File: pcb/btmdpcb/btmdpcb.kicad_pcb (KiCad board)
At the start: 2 copper layers, 51 parts, among them J2 ANT, Q1 BSD235C, Q2 2N7000, Q3 2N7000, Q4 BSD235C, Q5 AO3401A, Q6 BSD235C, Q7 2N7000, Q8 BSD235N, T1 ED8_4, T2 ED8_4, U2 TP4057, U3 ME6211C33M5

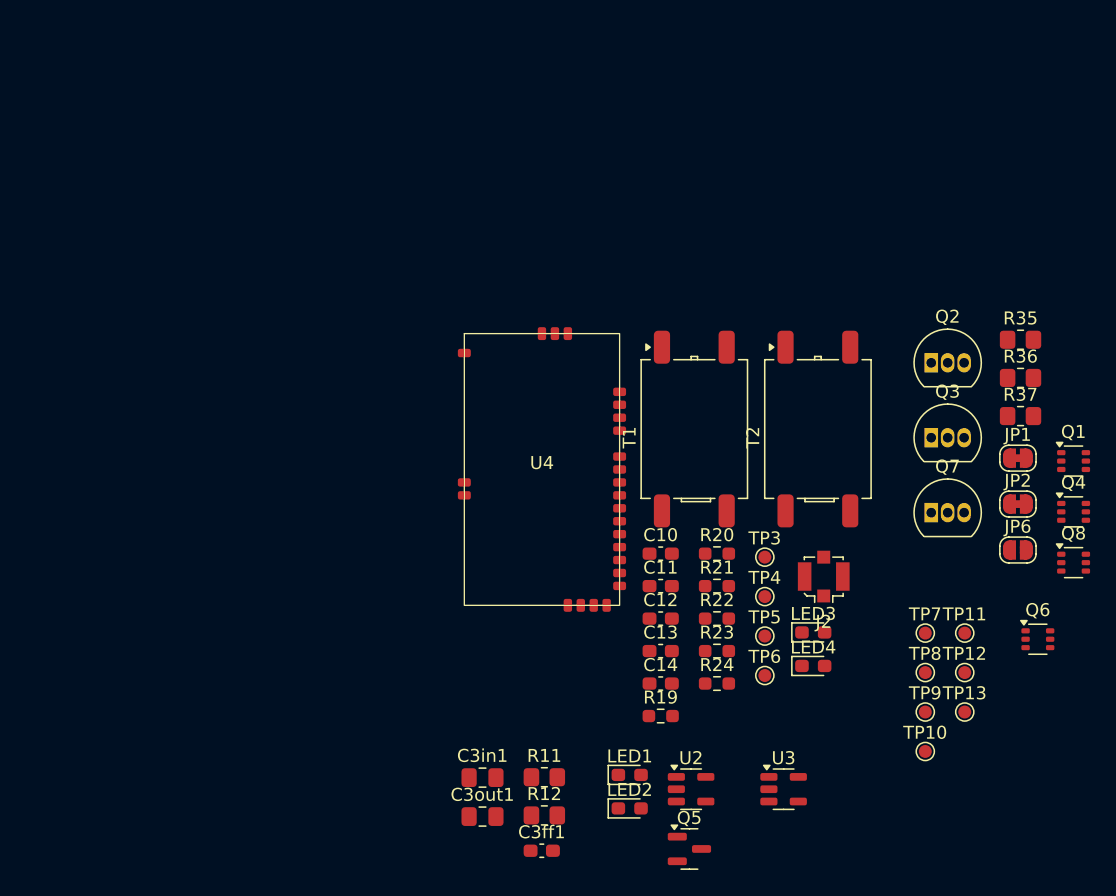
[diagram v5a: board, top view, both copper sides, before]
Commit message: Add missing libraries, assign all footprints
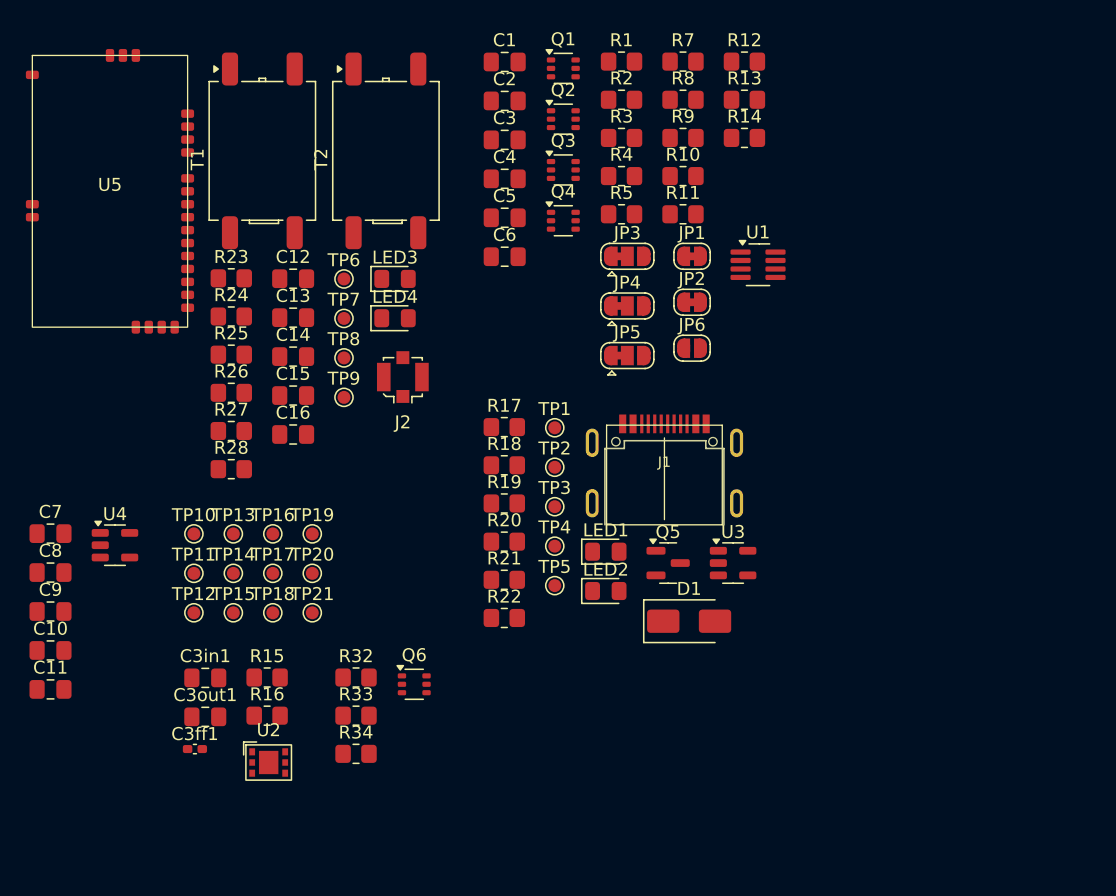
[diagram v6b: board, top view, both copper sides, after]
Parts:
- removed Q7: 2N7000, Package_TO_SOT_THT:TO-92_Inline
- removed Q8: BSD235N, Package_TO_SOT_SMD:SOT-363_SC-70-6
- removed R35, R36, R37: R, Resistor_SMD:R_0805_2012Metric_Pad1.20x1.40mm_HandSolder
- added C1: C, Capacitor_SMD:C_0805_2012Metric_Pad1.18x1.45mm_HandSolder, F.Cu at (62.5, 25.9)
- added C15: 1u, Capacitor_SMD:C_0805_2012Metric_Pad1.18x1.45mm_HandSolder, F.Cu at (46.1, 51.6)
- added C16: 100n, Capacitor_SMD:C_0805_2012Metric_Pad1.18x1.45mm_HandSolder, F.Cu at (46.1, 54.6)
- added C2: 1u, Capacitor_SMD:C_0805_2012Metric_Pad1.18x1.45mm_HandSolder, F.Cu at (62.5, 28.9)
- added C3: 10u, Capacitor_SMD:C_0805_2012Metric_Pad1.18x1.45mm_HandSolder, F.Cu at (62.5, 31.9)
- added C4: 100n, Capacitor_SMD:C_0805_2012Metric_Pad1.18x1.45mm_HandSolder, F.Cu at (62.5, 34.9)
- added C5: 100n, Capacitor_SMD:C_0805_2012Metric_Pad1.18x1.45mm_HandSolder, F.Cu at (62.5, 37.9)
- added C6: 1u or more, Capacitor_SMD:C_0805_2012Metric_Pad1.18x1.45mm_HandSolder, F.Cu at (62.5, 40.9)
- added C7: 10u, Capacitor_SMD:C_0805_2012Metric_Pad1.18x1.45mm_HandSolder, F.Cu at (27.4, 62.3)
- added C8: 100n, Capacitor_SMD:C_0805_2012Metric_Pad1.18x1.45mm_HandSolder, F.Cu at (27.4, 65.3)
- added C9: 1u, Capacitor_SMD:C_0805_2012Metric_Pad1.18x1.45mm_HandSolder, F.Cu at (27.4, 68.3)
- added D1: GS1A, Diode_SMD:D_SMA, F.Cu at (76.7, 69.1)
- added J1: USB_C_Receptacle_USB2.0_14P, usb:TYPE-C-31-M-14, F.Cu at (74.8, 58.9)
- added JP3: SolderJumper_3_Bridged12, Jumper:SolderJumper-3_P1.3mm_Bridged12_RoundedPad1.0x1.5mm, F.Cu at (72.0, 40.9)
- added JP4: SolderJumper_3_Bridged12, Jumper:SolderJumper-3_P1.3mm_Bridged12_RoundedPad1.0x1.5mm, F.Cu at (72.0, 44.7)
- added JP5: SolderJumper_3_Bridged12, Jumper:SolderJumper-3_P1.3mm_Bridged12_RoundedPad1.0x1.5mm, F.Cu at (72.0, 48.5)
- added R1: 10k, Resistor_SMD:R_0805_2012Metric_Pad1.20x1.40mm_HandSolder, F.Cu at (71.5, 25.8)
- added R10: 100k, Resistor_SMD:R_0805_2012Metric_Pad1.20x1.40mm_HandSolder, F.Cu at (76.3, 34.7)
- added R13: 100k, Resistor_SMD:R_0805_2012Metric_Pad1.20x1.40mm_HandSolder, F.Cu at (81.0, 28.8)
- added R14: 100k, Resistor_SMD:R_0805_2012Metric_Pad1.20x1.40mm_HandSolder, F.Cu at (81.0, 31.7)
- added R15: 100k, Resistor_SMD:R_0805_2012Metric_Pad1.20x1.40mm_HandSolder, F.Cu at (44.1, 73.4)
- added R16: 115k, Resistor_SMD:R_0805_2012Metric_Pad1.20x1.40mm_HandSolder, F.Cu at (44.1, 76.4)
- added R17: 5k1, Resistor_SMD:R_0805_2012Metric_Pad1.20x1.40mm_HandSolder, F.Cu at (62.5, 54.1)
- added R18: 5k1, Resistor_SMD:R_0805_2012Metric_Pad1.20x1.40mm_HandSolder, F.Cu at (62.5, 57.0)
- added R2: 10k, Resistor_SMD:R_0805_2012Metric_Pad1.20x1.40mm_HandSolder, F.Cu at (71.5, 28.8)
- added R25: 5k1, Resistor_SMD:R_0805_2012Metric_Pad1.20x1.40mm_HandSolder, F.Cu at (41.4, 48.5)
- added R26: 5k1, Resistor_SMD:R_0805_2012Metric_Pad1.20x1.40mm_HandSolder, F.Cu at (41.4, 51.4)
- added R27: 100R, Resistor_SMD:R_0805_2012Metric_Pad1.20x1.40mm_HandSolder, F.Cu at (41.4, 54.4)
- added R28: 100R, Resistor_SMD:R_0805_2012Metric_Pad1.20x1.40mm_HandSolder, F.Cu at (41.4, 57.3)
- added R3: 330k, Resistor_SMD:R_0805_2012Metric_Pad1.20x1.40mm_HandSolder, F.Cu at (71.5, 31.7)
- added R32: 100k, Resistor_SMD:R_0805_2012Metric_Pad1.20x1.40mm_HandSolder, F.Cu at (51.0, 73.4)
- added R33: 100k, Resistor_SMD:R_0805_2012Metric_Pad1.20x1.40mm_HandSolder, F.Cu at (51.0, 76.4)
- added R34: 100k, Resistor_SMD:R_0805_2012Metric_Pad1.20x1.40mm_HandSolder, F.Cu at (51.0, 79.3)
- added R4: 150k, Resistor_SMD:R_0805_2012Metric_Pad1.20x1.40mm_HandSolder, F.Cu at (71.5, 34.7)
- added R5: 220k, Resistor_SMD:R_0805_2012Metric_Pad1.20x1.40mm_HandSolder, F.Cu at (71.5, 37.6)
- added R7: 100k, Resistor_SMD:R_0805_2012Metric_Pad1.20x1.40mm_HandSolder, F.Cu at (76.3, 25.8)
- added R8: 100k, Resistor_SMD:R_0805_2012Metric_Pad1.20x1.40mm_HandSolder, F.Cu at (76.3, 28.8)
- added R9: 10k, Resistor_SMD:R_0805_2012Metric_Pad1.20x1.40mm_HandSolder, F.Cu at (76.3, 31.7)
- added TP1: VUSB, TestPoint:TestPoint_Pad_D1.0mm, F.Cu at (66.4, 54.1)
- added TP14: TestPoint, TestPoint:TestPoint_Pad_D1.0mm, F.Cu at (41.5, 65.4)
- added TP15: TestPoint, TestPoint:TestPoint_Pad_D1.0mm, F.Cu at (41.5, 68.4)
- added TP16: TestPoint, TestPoint:TestPoint_Pad_D1.0mm, F.Cu at (44.6, 62.3)
- added TP17: TestPoint, TestPoint:TestPoint_Pad_D1.0mm, F.Cu at (44.6, 65.4)
- added TP18: TestPoint, TestPoint:TestPoint_Pad_D1.0mm, F.Cu at (44.6, 68.4)
- added TP19: TestPoint, TestPoint:TestPoint_Pad_D1.0mm, F.Cu at (47.6, 62.3)
- added TP2: VUSB, TestPoint:TestPoint_Pad_D1.0mm, F.Cu at (66.4, 57.2)
- added TP20: TestPoint, TestPoint:TestPoint_Pad_D1.0mm, F.Cu at (47.6, 65.4)
- added TP21: TestPoint, TestPoint:TestPoint_Pad_D1.0mm, F.Cu at (47.6, 68.4)
- added U1: LM393, Package_TO_SOT_SMD:SOT-23-8_Handsoldering, F.Cu at (82.1, 41.5)
- added U5: ~, bt_audio:bt_audio_smd, F.Cu at (32.0, 35.9)
- C10, C12, C13: footprint Capacitor_SMD:C_0603_1608Metric_Pad1.08x0.95mm_HandSolder -> Capacitor_SMD:C_0805_2012Metric_Pad1.18x1.45mm_HandSolder
- C11: value 1u -> 100n; footprint Capacitor_SMD:C_0603_1608Metric_Pad1.08x0.95mm_HandSolder -> Capacitor_SMD:C_0805_2012Metric_Pad1.18x1.45mm_HandSolder
- C14: value 100n -> 1u; footprint Capacitor_SMD:C_0603_1608Metric_Pad1.08x0.95mm_HandSolder -> Capacitor_SMD:C_0805_2012Metric_Pad1.18x1.45mm_HandSolder
- C3ff1: footprint Capacitor_SMD:C_0603_1608Metric_Pad1.08x0.95mm_HandSolder -> Capacitor_SMD:C_0402_1005Metric_Pad0.74x0.62mm_HandSolder
- LED1, LED2, LED3, LED4: footprint LED_SMD:LED_0603_1608Metric_Pad1.05x0.95mm_HandSolder -> LED_SMD:LED_0805_2012Metric_Pad1.15x1.40mm_HandSolder
- Q1: value BSD235C -> BSD235N
- Q2: value 2N7000 -> BSD235C; footprint Package_TO_SOT_THT:TO-92_Inline -> Package_TO_SOT_SMD:SOT-363_SC-70-6
- Q3: value 2N7000 -> BSD235N; footprint Package_TO_SOT_THT:TO-92_Inline -> Package_TO_SOT_SMD:SOT-363_SC-70-6
- R12: value 115k -> 100k
- R19, R20: value 5k1 -> 330R; footprint Resistor_SMD:R_0603_1608Metric_Pad0.98x0.95mm_HandSolder -> Resistor_SMD:R_0805_2012Metric_Pad1.20x1.40mm_HandSolder
- R21: value 5k1 -> TBD; footprint Resistor_SMD:R_0603_1608Metric_Pad0.98x0.95mm_HandSolder -> Resistor_SMD:R_0805_2012Metric_Pad1.20x1.40mm_HandSolder
- R22: value 5k1 -> 100k; footprint Resistor_SMD:R_0603_1608Metric_Pad0.98x0.95mm_HandSolder -> Resistor_SMD:R_0805_2012Metric_Pad1.20x1.40mm_HandSolder
- R23, R24: value 100R -> 5k1; footprint Resistor_SMD:R_0603_1608Metric_Pad0.98x0.95mm_HandSolder -> Resistor_SMD:R_0805_2012Metric_Pad1.20x1.40mm_HandSolder
- TP3: value TestPoint -> VUSB
- TP4: value TestPoint -> BAT+
- TP5: value LED1 -> BAT-
- TP6: value LED2 -> TestPoint
- TP8: value TestPoint -> LED1
- TP9: value TestPoint -> LED2
- U2: value TP4057 -> Würth 171010502; footprint Package_TO_SOT_SMD:TSOT-23-5 -> MagIC_SMD_Wurth:U_Wurth_WPME-VDMM_171010502
- U3: value ME6211C33M5 -> TP4057; footprint Package_TO_SOT_SMD:SOT-23-5 -> Package_TO_SOT_SMD:TSOT-23-5
- U4: value ~ -> ME6211C33M5; footprint bt_audio:bt_audio_smd -> Package_TO_SOT_SMD:SOT-23-5
- moved R12 60.3 mm to (81.0, 25.8)
- moved TP11 59.8 mm to (38.5, 65.4)
- moved TP12 59.8 mm to (38.5, 68.4)
- moved TP10 59.0 mm to (38.5, 62.3)
- moved TP13 58.2 mm to (41.5, 62.3)
- moved TP7 51.1 mm to (50.1, 45.7)
- moved TP8 51.1 mm to (50.1, 48.7)
- moved TP9 51.1 mm to (50.1, 51.8)
- moved Q1 49.8 mm to (67.0, 26.4)
- moved Q6 48.3 mm to (55.5, 74.0)
- moved C11 47.8 mm to (27.4, 74.3)
- moved C10 47.7 mm to (27.4, 71.3)
- moved R23 47.3 mm to (41.4, 42.6)
- moved R24 47.0 mm to (41.4, 45.5)
- moved Q4 45.4 mm to (67.0, 38.1)
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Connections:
- C10 pad 1: Net-(C10-Pad1) -> +3V3
- C10 pad 2: Net-(U4-L+) -> GND
- C11 pad 1: Net-(C11-Pad1) -> +3V3
- C11 pad 2: Net-(U4-L-) -> GND
- C12 pad 2: Net-(U4-R-) -> Net-(U5-L+)
- C13 pad 2: Net-(U4-R+) -> Net-(U5-L-)
- C14 pad 1: +3V3 -> Net-(C14-Pad1)
- C14 pad 2: GND -> Net-(U5-R-)
- C3ff1 pad 2: Net-(U1-FB) -> Net-(U2-FB)
- Q1 pad 2: /HOLD -> Net-(Q1A-G1)
- Q1 pad 3: /REC -> unconnected-(Q1B-D2-Pad3)
- Q1 pad 4: +BATT -> unconnected-(Q1B-S2-Pad4)
- Q1 pad 5: /~{REC} -> unconnected-(Q1B-G2-Pad5)
- Q1 pad 6: /KICKSTART/BT_BTN -> Net-(Q1A-D1)
- Q2 pad 2: /KICKSTART/BT_BTN -> /HOLD
- Q2 pad 3: ~{EN_1V5} -> /REC
- Q3 pad 2: VDD -> /KICKSTART/BT_BTN
- Q5 pad 3: Net-(BT1-+) -> Net-(Q5-D)
- R11 pad 1: +1V5 -> VDD
- R11 pad 2: Net-(U1-FB) -> GND
- R12 pad 1: Net-(U1-FB) -> +BATT
- R12 pad 2: GND -> ~{EN_1V5}
- R19 pad 1: Net-(R19-Pad1) -> VBUS
- R19 pad 2: Net-(C10-Pad1) -> Net-(LED1-A)
- R20 pad 1: Net-(R20-Pad1) -> VBUS
- R20 pad 2: Net-(C11-Pad1) -> Net-(LED2-A)
- R21 pad 1: Net-(R21-Pad1) -> Net-(U3-PROG)
- R21 pad 2: Net-(C12-Pad1) -> GND
- R22 pad 1: Net-(R22-Pad1) -> VBUS
- R22 pad 2: Net-(C13-Pad1) -> GND
- R23 pad 1: Net-(U4-LED1) -> Net-(R23-Pad1)
- R23 pad 2: Net-(LED3-K) -> Net-(C12-Pad1)
- R24 pad 1: Net-(U4-LED2) -> Net-(R24-Pad1)
- R24 pad 2: Net-(LED4-K) -> Net-(C13-Pad1)
- T1 pad 3: Net-(R20-Pad1) -> Net-(R24-Pad1)
- T1 pad 4: Net-(R19-Pad1) -> Net-(R23-Pad1)
- T2 pad 3: Net-(R21-Pad1) -> Net-(R25-Pad1)
- T2 pad 4: Net-(R22-Pad1) -> Net-(R26-Pad1)
- TP10 pad 1: /MD unit (MZ-N505)/~{BTN_REC}_IN -> +1V5
- TP11 pad 1: /MD unit (MZ-N505)/~{BTN_PAUSE}_IN -> GND
- TP12 pad 1: /~{REC} -> /MD unit (MZ-N505)/~{BTN_PAUSE}_IN
- TP13 pad 1: /~{HOLD} -> /MD unit (MZ-N505)/~{SW_HOLD}_IN
- TP3 pad 1: Net-(U4-BAT+) -> VBUS
- TP4 pad 1: /bt_module/PWR_EN -> Net-(Q5-D)
- TP5 pad 1: Net-(LED3-K) -> GND
- TP6 pad 1: Net-(LED4-K) -> Net-(U5-BAT+)
- TP7 pad 1: /MD unit (MZ-N505)/~{BTN_PAUSE}_IN -> /bt_module/PWR_EN
- TP8 pad 1: /MD unit (MZ-N505)/~{SW_HOLD}_IN -> Net-(LED3-K)
- TP9 pad 1: VDD -> Net-(LED4-K)
- U2 pad 1: Net-(LED2-K) -> +1V5
- U2 pad 2: GND -> /power_we/MODE
- U2 pad 3: Net-(BT1-+) -> Net-(U2-FB)
- U2 pad 4: VBUS -> /power_we/Vin
- U2 pad 5: Net-(LED1-K) -> /power_we/EN
- U3 pad 1: /power_3v3/Vin -> Net-(LED2-K)
- U3 pad 3: /power_3v3/EN -> Net-(Q5-D)
- U3 pad 4: unconnected-(U3-NC-Pad4) -> VBUS
- U3 pad 5: +3V3 -> Net-(LED1-K)
- U4 pad 1: GND -> /power_3v3/Vin
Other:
- board outline added: 9.2 x 6.5 mm

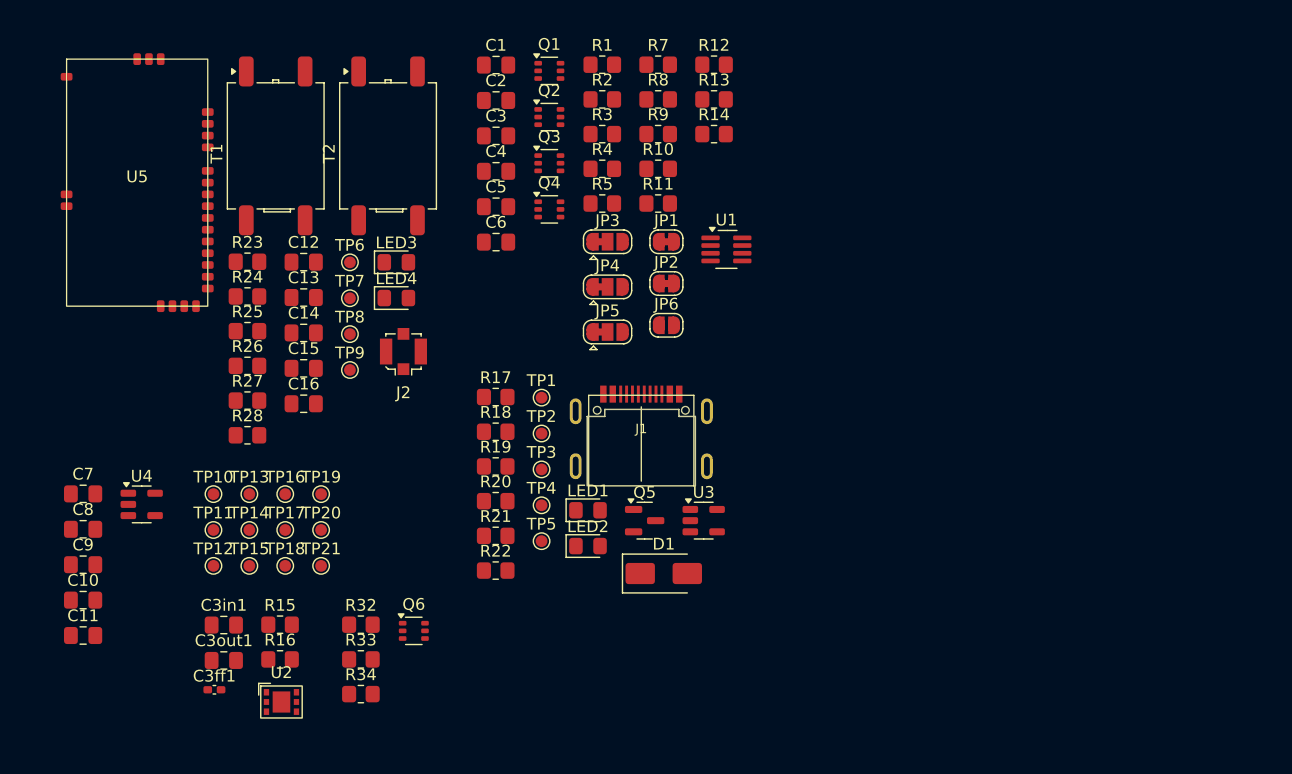
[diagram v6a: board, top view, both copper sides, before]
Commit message: Correct footprints, fix issues on update PCB from schematic
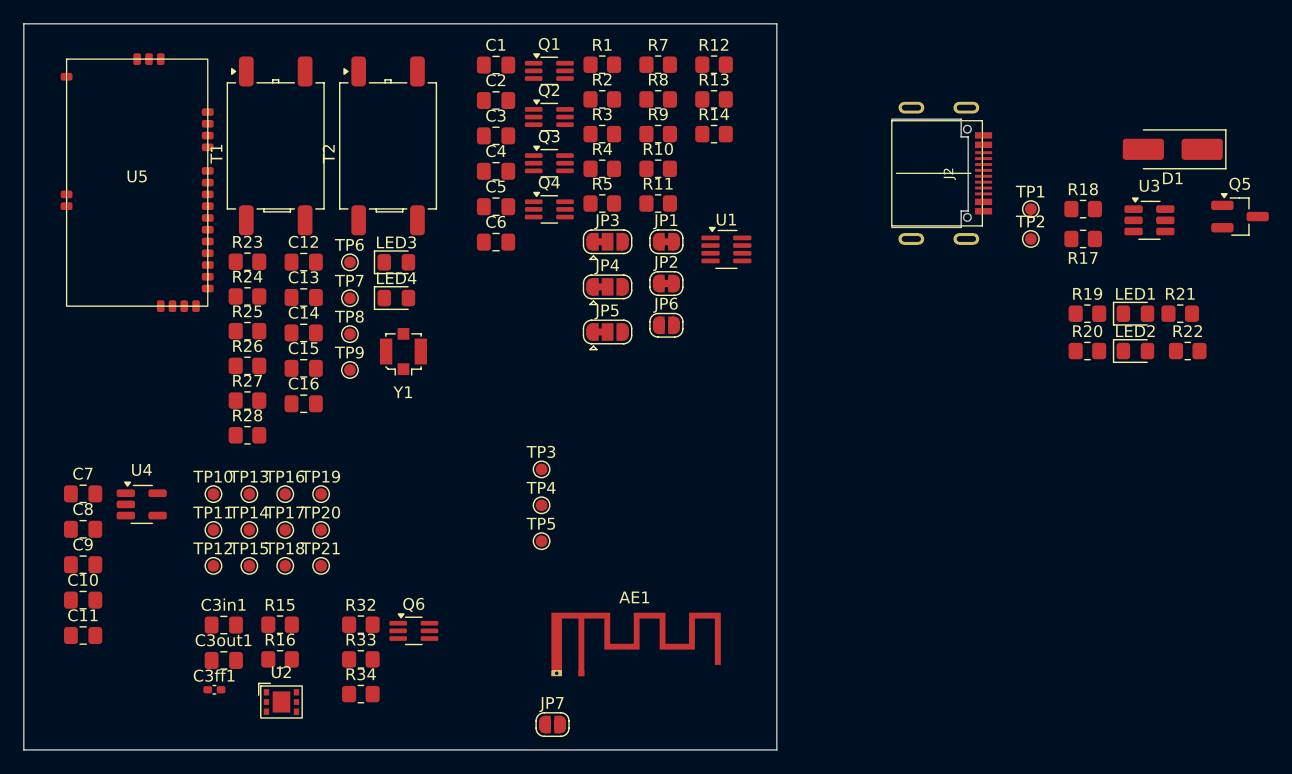
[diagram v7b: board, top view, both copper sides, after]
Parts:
- removed J1: USB_C_Receptacle_USB2.0_14P, usb:TYPE-C-31-M-14
- added AE1: Antenna_Shield, RF_Antenna:Texas_SWRA117D_2.4GHz_Right, F.Cu at (69.7, 77.6)
- added J2: USB_C_Receptacle_USB2.0_16P, usb:TYPE-C-31-M-14, F.Cu at (98.8, 35.1)
- added JP7: SolderJumper_2_Open, Jumper:SolderJumper-2_P1.3mm_Open_RoundedPad1.0x1.5mm, F.Cu at (67.3, 81.9)
- D1: footprint Diode_SMD:D_SMA -> Diode_SMD:D_SMA_Handsoldering
- Q1, Q2, Q3, Q4, Q6: footprint Package_TO_SOT_SMD:SOT-363_SC-70-6 -> Package_TO_SOT_SMD:SOT-363_SC-70-6_Handsoldering
- Q5: footprint Package_TO_SOT_SMD:SOT-23 -> Package_TO_SOT_SMD:SOT-23_Handsoldering
- U3: footprint Package_TO_SOT_SMD:TSOT-23-5 -> Package_TO_SOT_SMD:SOT-23-6_Handsoldering
- U4: footprint Package_TO_SOT_SMD:SOT-23-5 -> Package_TO_SOT_SMD:SOT-23-5_HandSoldering
- moved R22 61.7 mm to (121.3, 50.2)
- moved R21 61.2 mm to (120.7, 47.0)
- moved Q5 56.8 mm to (125.7, 38.7)
- moved D1 56.3 mm to (120.0, 33.0), turned to 180 degrees
- moved R18 53.4 mm to (112.4, 38.1)
- moved R19 51.9 mm to (112.8, 47.0)
- moved R20 51.9 mm to (112.8, 50.2)
- moved R17 51.7 mm to (112.4, 40.6), turned to 180 degrees
- moved LED1 49.4 mm to (116.8, 47.0)
- moved LED2 49.4 mm to (116.8, 50.2)
- moved U3 45.7 mm to (118.0, 39.1)
- moved TP2 44.8 mm to (108.0, 40.6)
- moved TP1 44.6 mm to (108.0, 38.1)
- renumbered J2 to Y1
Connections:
- net Net-(Q5-D) renamed /supply/BAT+
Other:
- board size 9.2 x 6.5 mm -> 64 x 61.7 mm
- copper layers 2 -> 4

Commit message: Layout PCB
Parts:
- removed the C1 at (62.5, 25.9)
- removed the C5 at (62.5, 37.9)
- removed the TP12 at (38.5, 68.4)
- removed the TP15 at (41.5, 68.4)
- removed the TP19 at (47.6, 62.3)
- added C18: 100n, Capacitor_SMD:C_0805_2012Metric_Pad1.18x1.45mm_HandSolder, F.Cu at (145.4, 60.3)
- added C20: 100n, Capacitor_SMD:C_0805_2012Metric_Pad1.18x1.45mm_HandSolder, F.Cu at (158.8, 49.5)
- added C3: 10u, Capacitor_SMD:C_0805_2012Metric_Pad1.18x1.45mm_HandSolder, F.Cu at (115.6, 46.4)
- added JP10: L_SKIP, Jumper:SolderJumper-2_P1.3mm_Open_RoundedPad1.0x1.5mm, F.Cu at (130.2, 81.3)
- added JP12: USB_PWR, Jumper:SolderJumper-2_P1.3mm_Open_RoundedPad1.0x1.5mm, F.Cu at (140.8, 60.3)
- added JP7: SHLD2GND, Jumper:SolderJumper-2_P1.3mm_Open_RoundedPad1.0x1.5mm, F.Cu at (100.3, 59.1)
- added JP8: R_SKIP, Jumper:SolderJumper-2_P1.3mm_Open_RoundedPad1.0x1.5mm, F.Cu at (130.2, 68.6)
- added JP9: AGND_SKIP, Jumper:SolderJumper-3_P1.3mm_Open_RoundedPad1.0x1.5mm, F.Cu at (130.2, 74.9)
- added TP10: 3V3_IN, TestPoint:TestPoint_Pad_D1.0mm, F.Cu at (144.9, 45.1)
- added TP11: 3V3_OUT, TestPoint:TestPoint_Pad_D1.0mm, F.Cu at (144.9, 52.7)
- added TP22: BT_L+, TestPoint:TestPoint_Pad_D1.0mm, F.Cu at (148.6, 70.5)
- added TP23: BT_L-, TestPoint:TestPoint_Pad_D1.0mm, F.Cu at (148.6, 67.9)
- added TP24: BT_R-, TestPoint:TestPoint_Pad_D1.0mm, F.Cu at (148.6, 65.4)
- added TP25: BT_R+, TestPoint:TestPoint_Pad_D1.0mm, F.Cu at (148.6, 62.9)
- added TP26: BT_USB_IN, TestPoint:TestPoint_Pad_D1.0mm, F.Cu at (148.6, 60.3)
- added TP27: BT_3V3, TestPoint:TestPoint_Pad_D1.0mm, F.Cu at (165.1, 64.1)
- added TP28: GND, TestPoint:TestPoint_Pad_D1.0mm, F.Cu at (165.1, 54.6)
- added TP29: BT_BTN, TestPoint:TestPoint_Pad_D1.0mm, F.Cu at (154.9, 49.5)
- added TP3: GND, TestPoint:TestPoint_Pad_D1.0mm, F.Cu at (109.2, 61.6)
- added TP7: VSUPPLY, TestPoint:TestPoint_Pad_D1.0mm, F.Cu at (128.3, 49.5)
- added TP8: 1V5_IN, TestPoint:TestPoint_Pad_D1.0mm, F.Cu at (126.2, 58.3)
- added TP9: 1V5_OUT, TestPoint:TestPoint_Pad_D1.0mm, F.Cu at (134.2, 57.0)
- AE1: footprint RF_Antenna:Texas_SWRA117D_2.4GHz_Right -> RF_Antenna:Texas_SWRA117D_2.4GHz_Left
- C4: value 100n -> 10u
- C6: value 1u or more -> 1u
- JP1: value SolderJumper_2_Bridged -> 1V5_IN
- JP11: renamed from JP7; value SolderJumper_2_Open -> ANT
- JP2: value SolderJumper_2_Bridged -> 3V3_IN
- JP3: value SolderJumper_3_Bridged12 -> 1V5_EN
- JP4: value SolderJumper_3_Bridged12 -> 3V3_EN
- JP5: value SolderJumper_3_Bridged12 -> 3V3_MODE
- JP6: value SolderJumper_2_Open -> VBUS_EN
- R19: renamed from R21; value TBD -> 1k6
- TP1: value VUSB -> D-
- TP12: renamed from TP10; value TestPoint -> 1V5
- TP13: renamed from TP11; value TestPoint -> GND
- TP15: renamed from TP13; value TestPoint -> HOLD
- TP16: renamed from TP17; value TestPoint -> L
- TP17: renamed from TP16; value TestPoint -> R
- TP18: value TestPoint -> AGND
- TP19: renamed from TP14; value TestPoint -> DVDD
- TP2: value VUSB -> D+
- TP20: value TestPoint -> REC
- TP21: value TestPoint -> HOLD
- TP30: renamed from TP8; value LED1 -> BT_LED1
- TP31: renamed from TP9; value LED2 -> BT_LED2
- TP32: renamed from TP6; value TestPoint -> BT_BAT+
- TP33: renamed from TP7; value TestPoint -> BT_CE
- TP5: renamed from TP4; value BAT+ -> +
- TP6: renamed from TP5; value BAT- -> -
- moved U5 127.6 mm to (156.8, 62.2), turned to 180 degrees
- moved C13 120.8 mm to (145.5, 48.9), turned to -90 degrees
- moved C19 119.1 mm to (165.1, 60.3), turned to 90 degrees
- moved C12 115.2 mm to (141.1, 52.7)
- moved C9 115.0 mm to (141.1, 45.1)
- moved C10 111.1 mm to (136.6, 45.1)
- moved C11 110.3 mm to (136.6, 52.7), turned to 180 degrees
- moved U4 109.0 mm to (140.4, 48.9)
- moved Y1 107.3 mm to (158.8, 76.2), turned to -90 degrees
- moved R29 104.1 mm to (145.4, 55.2), turned to 180 degrees
- moved R30 104.1 mm to (145.4, 57.8)
- moved R25 103.4 mm to (141.0, 70.5)
- moved C14 103.1 mm to (145.4, 70.5)
- moved TP32 102.6 mm to (152.4, 49.5), turned to 180 degrees
- moved R26 102.1 mm to (141.0, 67.9)
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- renumbered C2 to C1, C8 to C10, C9 to C11, C10 to C12, C11 to C13, C12 to C14, C13 to C15, C14 to C16, C15 to C17, C16 to C19, C3 to C2, C3in1 to C5, C3ff1 to C7, C3out1 to C8, C7 to C9, J2 to J1, R17 to R15, R18 to R16, R19 to R17, R20 to R18, R22 to R20, R15 to R21, R16 to R22, R23 to R25, R24 to R26, R25 to R27, R26 to R28, R27 to R29, R28 to R30, R32 to R31, R33 to R32, R34 to R33, T2 to T1, T1 to T2, TP3 to TP4, U3 to U2, U2 to U3
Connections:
- net Net-(J2-CC1) renamed /supply/CC1
- net Net-(J2-CC2) renamed /supply/CC2
- net Net-(J2-D+-PadA6) renamed /supply/D+
- net Net-(J2-D--PadA7) renamed /supply/D-
- C4 pad 1: GND -> /supply/BAT+
- C4 pad 2: /KICKSTART/BT_BTN -> GND
- C6 pad 1: +3V3 -> /power_we/EN
- D1 pad 1: +BATT -> +SUPPLY
- J1 pad S1: GND -> /supply/SHIELD
- JP1 pad 1: +BATT -> +SUPPLY
- JP2 pad 1: +BATT -> +SUPPLY
- Q2 pad 4: +BATT -> +SUPPLY
- Q4 pad 4: +BATT -> +SUPPLY
- Q5 pad 2: +BATT -> +SUPPLY
- Q6 pad 4: +BATT -> +SUPPLY
- R12 pad 1: +BATT -> +SUPPLY
- R27 pad 1: Net-(R25-Pad1) -> Net-(JP9-B)
- R28 pad 1: Net-(R26-Pad1) -> Net-(JP8-B)
- R3 pad 1: +3V3 -> +SUPPLY
- R30 pad 1: Net-(U5-LED2) -> Net-(LED4-K)
- R30 pad 2: Net-(LED4-K) -> Net-(U5-LED2)
- R31 pad 2: +BATT -> +SUPPLY
- R4 pad 1: +3V3 -> +SUPPLY
- R7 pad 2: +BATT -> +SUPPLY
- T1 pad 1: /MD unit (MZ-N505)/AUDIO_R -> Net-(JP8-B)
- T1 pad 2: /MD unit (MZ-N505)/AUDIO_GND -> Net-(JP9-B)
- T1 pad 3: Net-(R25-Pad1) -> /MD unit (MZ-N505)/AUDIO_GND
- T1 pad 4: Net-(R26-Pad1) -> /MD unit (MZ-N505)/AUDIO_R
- TP30 pad 1: Net-(LED3-K) -> Net-(U5-LED1)
- TP31 pad 1: Net-(LED4-K) -> Net-(U5-LED2)
- U5 pad 37: unconnected-(U5-USB_IN-Pad37) -> Net-(JP12-B)
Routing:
- net +3V3: track 0.00 -> 100.8 mm
- net +SUPPLY: track 0.00 -> 87.2 mm, vias 0 -> 8
- net /KICKSTART/BT_BTN: track 0.00 -> 76.9 mm, vias 0 -> 2
- net +1V5: track 0.00 -> 59.2 mm, vias 0 -> 2
- net VBUS: track 0.00 -> 57.9 mm, vias 0 -> 4
- net VDD: track 0.00 -> 52.7 mm, vias 0 -> 2
- net EN_1V5: track 0.00 -> 32.6 mm
- net GND: track 0.00 -> 25.7 mm, vias 0 -> 69
- net /MD unit (MZ-N505)/AUDIO_R: track 0.00 -> 24.1 mm
- net /power_3v3/Vin: track 0.00 -> 20.0 mm
- net /MD unit (MZ-N505)/AUDIO_GND: track 0.00 -> 18.9 mm
- net Net-(JP10-B): track 0.00 -> 18.8 mm
- net Net-(JP9-A): track 0.00 -> 17.0 mm
- net Net-(JP9-B): track 0.00 -> 15.6 mm
- net /~{REC}: track 0.00 -> 13.7 mm
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- added copper zone on B.Cu, net /supply/SHIELD
- added copper zone on F.Cu, net /supply/SHIELD
- added copper zone on B.Cu, net GND
- added copper zone on F.Cu, net GND
- added copper zone on In1.Cu, net GND
- added copper zone on In2.Cu, net GND
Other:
- board size 64 x 61.7 mm -> 72.4 x 44.4 mm
- board text added: ">"
- board text added: "BAT"
- board text added: "BTMD v0.4 eval 2025-04 D. Rojas"
- board text added: "MD"
